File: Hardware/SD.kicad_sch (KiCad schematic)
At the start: 2 parts, among them J1 ST1W008S4TR2000

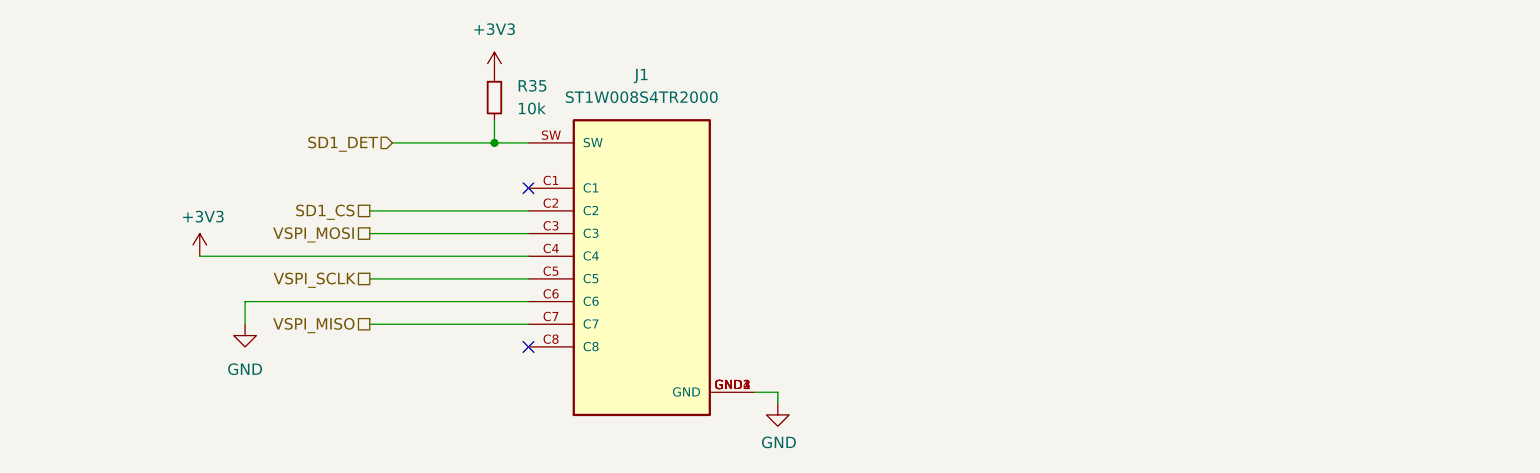
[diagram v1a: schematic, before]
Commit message: SD card fix + logos
Changed SD card from the lock in to the push in
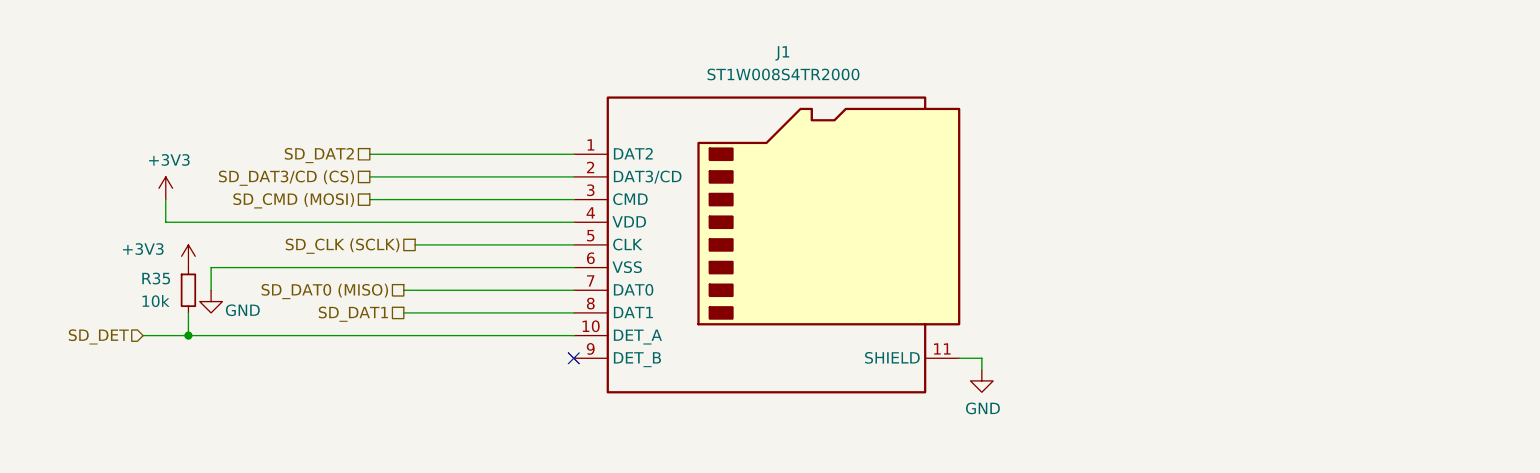
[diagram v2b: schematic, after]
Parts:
- J1: footprint iclr:JAE_ST1W008S4TR2000 -> Connector_Card:microSD_HC_Hirose_DM3AT-SF-PEJM5; symbol iclr-hw:ST1W008S4TR2000 -> Connector:Micro_SD_Card_Det_Hirose_DM3AT
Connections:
- net +3V3: now also J1.4 (VDD); no longer J1.C4
- net GND: now also J1.11 (SHIELD), J1.6 (VSS); no longer J1.C6, J1.GND1 (GND), J1.GND2 (GND), J1.GND3 (GND), J1.GND4 (GND)
- removed net SD1_CS: J1.C2
- net SD1_DET renamed SD_DET
- net SD_DET: now also J1.10 (DET_A); no longer J1.SW
- removed net VSPI_MISO: J1.C7
- removed net VSPI_MOSI: J1.C3
- removed net VSPI_SCLK: J1.C5
- new net SD_CLK (SCLK): J1.5 (CLK)
- new net SD_CMD (MOSI): J1.3 (CMD)
- new net SD_DAT0 (MISO): J1.7 (DAT0)
- new net SD_DAT1: J1.8 (DAT1)
- new net SD_DAT2: J1.1 (DAT2)
- new net SD_DAT3/CD (CS): J1.2 (DAT3/CD)
- no-connect marks 2 -> 1
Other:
- moved on the sheet: R35

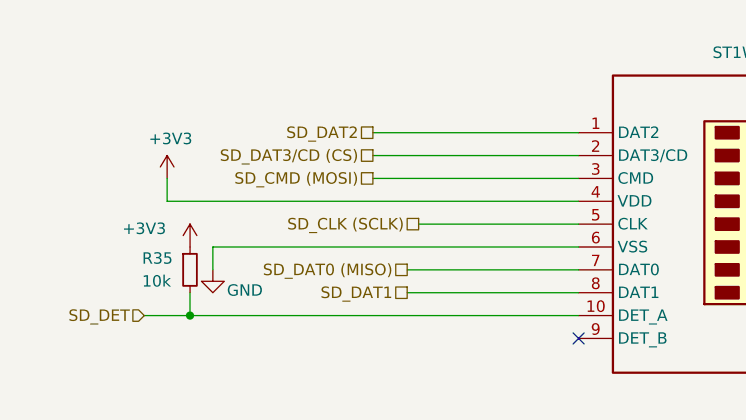
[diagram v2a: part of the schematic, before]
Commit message: Crosshair post review 2
Layout redesign + changes implemented. Traces not yet complete
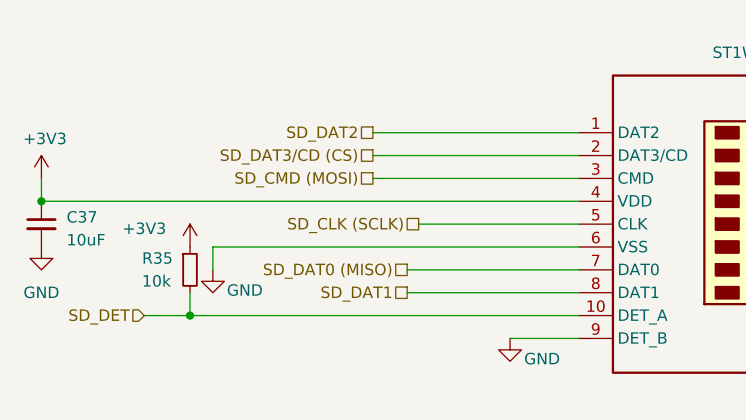
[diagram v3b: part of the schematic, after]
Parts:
- added C37: 10uF, Capacitor_SMD:C_0402_1005Metric, symbol Device:C_Small
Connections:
- net +3V3: now also C37.1
- net GND: now also J1.9 (DET_B), C37.2
- no-connect marks 1 -> 0
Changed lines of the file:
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@@
 		(color 0 0 0 0)
 	)
-	(no_connect
-		(at 137.16 110.49)
+	(junction
+		(at 77.47 95.25)
+		(diameter 0)
+		(color 0 0 0 0)
 	)
 	(wire
@@
 	(wire
 		(pts
-			(xy 91.44 95.25) (xy 137.16 95.25)
+			(xy 129.54 110.49) (xy 137.16 110.49)
+		)
+		(stroke
+			(width 0)
+			(type default)
+		)
+	)
+	(wire
+		(pts
+			(xy 77.47 95.25) (xy 137.16 95.25)
 		)
 		(stroke
@@
 	(wire
 		(pts
-			(xy 91.44 95.25) (xy 91.44 92.71)
+			(xy 77.47 95.25) (xy 77.47 92.71)
 		)
 		(stroke
@@
 	(symbol
 		(lib_id "power:+3.3V")
-		(at 91.44 92.71 0)
+		(at 77.47 92.71 0)
 		(unit 1)
 		(exclude_from_sim no)
@@
 		(dnp no)
 		(property "Reference" "#PWR017"
-			(at 91.44 96.52 0)
+			(at 77.47 96.52 0)
 			(effects
 				(font
@@
 		)
 		(property "Value" "+3V3"
-			(at 91.821 88.3158 0)
+			(at 77.851 88.3158 0)
 			(effects
 				(font
@@
 		)
 		(property "Footprint" ""
-			(at 91.44 92.71 0)
+			(at 77.47 92.71 0)
 			(effects
 				(font
@@
 		)
 		(property "Datasheet" ""
-			(at 91.44 92.71 0)
+			(at 77.47 92.71 0)
 			(effects
 				(font
@@
 		)
 		(property "Description" ""
-			(at 91.44 92.71 0)
+			(at 77.47 92.71 0)
 			(effects
 				(font
@@
 				(path "/7db990e4-92e1-4f99-b4d2-435bbec1ba83/9b3767b0-c58a-45b6-92e7-d7216660795a"
 					(reference "#PWR017")
+					(unit 1)
+				)
+			)
+		)
+	)
+	(symbol
+		(lib_id "power:GND")
+		(at 77.47 100.33 0)
+		(unit 1)
+		(exclude_from_sim no)
+		(in_bom yes)
+		(on_board yes)
+		(dnp no)
+		(fields_autoplaced yes)
+		(property "Reference" "#PWR087"
+			(at 77.47 106.68 0)
+			(effects
+				(font
+					(size 1.27 1.27)
+				)
+				(hide yes)
+			)
+		)
+		(property "Value" "GND"
+			(at 77.47 105.41 0)
+			(effects
+				(font
+					(size 1.27 1.27)
+				)
+			)
+		)
+		(property "Footprint" ""
+			(at 77.47 100.33 0)
+			(effects
+				(font
+					(size 1.27 1.27)
+				)
+				(hide yes)
+			)
+		)
+		(property "Datasheet" ""
+			(at 77.47 100.33 0)
+			(effects
+				(font
+					(size 1.27 1.27)
+				)
+				(hide yes)
+			)
+		)
+		(property "Description" "Power symbol creates a global label with name \"GND\" , ground"
+			(at 77.47 100.33 0)
+			(effects
+				(font
+					(size 1.27 1.27)
+				)
+				(hide yes)
+			)
+		)
+		(pin "1"
+		)
+		(instances
+			(project "Main board"
+				(path "/7db990e4-92e1-4f99-b4d2-435bbec1ba83/9b3767b0-c58a-45b6-92e7-d7216660795a"
+					(reference "#PWR087")
+					(unit 1)
+				)
+			)
+		)
+	)
+	(symbol
+		(lib_id "power:GND")
+		(at 129.54 110.49 0)
+		(unit 1)
+		(exclude_from_sim no)
+		(in_bom yes)
+		(on_board yes)
+		(dnp no)
+		(property "Reference" "#PWR077"
+			(at 129.54 116.84 0)
+			(effects
+				(font
+					(size 1.27 1.27)
+				)
+				(hide yes)
+			)
+		)
+		(property "Value" "GND"
+			(at 133.096 112.776 0)
+			(effects
+				(font
+					(size 1.27 1.27)
+				)
+			)
+		)
+		(property "Footprint" ""
+			(at 129.54 110.49 0)
+			(effects
+				(font
+					(size 1.27 1.27)
+				)
+				(hide yes)
+			)
+		)
+		(property "Datasheet" ""
+			(at 129.54 110.49 0)
+			(effects
+				(font
+					(size 1.27 1.27)
+				)
+				(hide yes)
+			)
+		)
+		(property "Description" ""
+			(at 129.54 110.49 0)
+			(effects
+				(font
+					(size 1.27 1.27)
+				)
+				(hide yes)
+			)
+		)
+		(pin "1"
+		)
+		(instances
+			(project "Main board"
+				(path "/7db990e4-92e1-4f99-b4d2-435bbec1ba83/9b3767b0-c58a-45b6-92e7-d7216660795a"
+					(reference "#PWR077")
 					(unit 1)
 				)
@@
 					(unit 1)
 				)
+			)
+		)
+	)
+	(symbol
+		(lib_id "Device:C_Small")
+		(at 77.47 97.79 0)
+		(unit 1)
+		(exclude_from_sim no)
+		(in_bom yes)
+		(on_board yes)
+		(dnp no)
+		(property "Reference" "C37"
+			(at 80.264 97.028 0)
+			(effects
+				(font
+					(size 1.27 1.27)
+				)
+				(justify left)
+			)
+		)
+		(property "Value" "10uF"
+			(at 80.264 99.568 0)
+			(effects
+				(font
+					(size 1.27 1.27)
+				)
+				(justify left)
+			)
+		)
+		(property "Footprint" "Capacitor_SMD:C_0402_1005Metric"
+			(at 77.47 97.79 0)
+			(effects
+				(font
+					(size 1.27 1.27)
+				)
+				(hide yes)
+			)
+		)
+		(property "Datasheet" "~"
+			(at 77.47 97.79 0)
+			(effects
+				(font
+					(size 1.27 1.27)
+				)
+				(hide yes)
+			)
+		)
+		(property "Description" "Unpolarized capacitor, small symbol"
+			(at 77.47 97.79 0)
+			(effects
+				(font
+					(size 1.27 1.27)
+				)
+				(hide yes)
+			)
+		)
+		(pin "1"
+		)
+		(pin "2"
+		)
+		(instances
+			(project "Main board"
+				(path "/7db990e4-92e1-4f99-b4d2-435bbec1ba83/9b3767b0-c58a-45b6-92e7-d7216660795a"
+					(reference "C37")
+					(unit 1)
+				)

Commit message: V2 changes, PCB finished
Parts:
- removed J1: ST1W008S4TR2000, Connector_Card:microSD_HC_Hirose_DM3AT-SF-PEJM5, symbol Connector:Micro_SD_Card_Det_Hirose_DM3AT
- added J1: DM3AT-SF-PEJM5_40_, iclr:DM3ATSFPEJM540, symbol iclr:DM3AT-SF-PEJM5_40_
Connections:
- net +3V3: now also J1.4 (VDD)
- net GND: now also J1.6 (VSS), J1.MP1, J1.MP2, J1.MP3, J1.MP4, J1.MP5
- net SD_CLK (SCLK): now also J1.5 (CLK)
- net SD_CMD (MOSI): now also J1.3 (CMD)
- net SD_DAT0 (MISO): now also J1.7 (DAT0)
- net SD_DAT1: now also J1.8 (DAT1)
- net SD_DAT2: now also J1.1 (DAT2)
- net SD_DAT3/CD (CS): now also J1.2 (CD/DAT3)
- net SD_DET: now also J1.CD1 (CARD_DETECT)
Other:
- moved on the sheet: C37, R35

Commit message: More V2 changes
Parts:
- added C19: 10uF, Capacitor_SMD:C_0402_1005Metric, symbol Device:C_Small
- C37: value 10uF -> 0.1uF
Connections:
- net +3V3: now also C19.1
- net GND: now also C19.2
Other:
- moved on the sheet: C37, R35

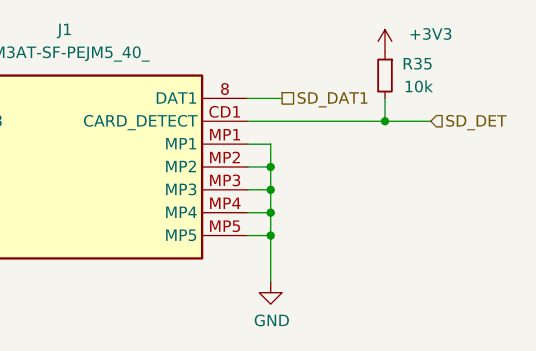
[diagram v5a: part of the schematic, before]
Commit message: More V2 changes
Mainly changed to use Ω symbol for resistors. Fixed the CDC pin for the buck boost
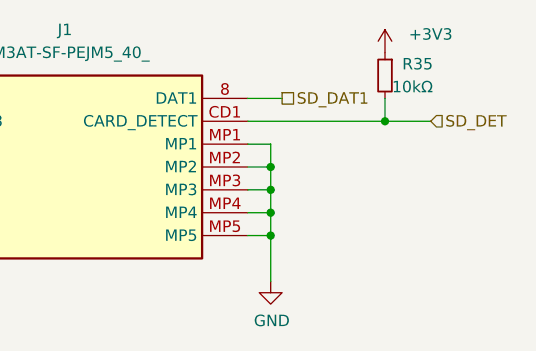
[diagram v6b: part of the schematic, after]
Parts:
- R35: value 10k -> 10kΩ
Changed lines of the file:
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@@
 			)
 		)
-		(property "Value" "10k"
+		(property "Value" "10kΩ"
 			(at 205.994 80.01 0)
 			(effects

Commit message: reformatted and renamed file
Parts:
- C1002: renamed from C37; value 0.1uF -> 100nF
- renumbered C19 to C1001, J1 to J1001, R35 to R1001
